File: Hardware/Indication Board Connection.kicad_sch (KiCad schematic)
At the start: 17 parts, among them J18 Conn_01x03, U11 TPS5405DR

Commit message: JLC Production Files
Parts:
- 5V_Buck1: LCSC (none) -> C7371904
- C26, C31, C32, C33: LCSC (none) -> C440198
- C27: LCSC (none) -> C15849
- C28: LCSC (none) -> C57112
- C29: LCSC (none) -> C107088
- C30: LCSC (none) -> C14663
- D27: LCSC (none) -> C41408002
- F1: LCSC (none) -> C269149
- R51: LCSC (none) -> C21190
- R64: LCSC (none) -> C137788
- U11: LCSC (none) -> C488409
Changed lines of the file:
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@@
+			)
+		)
+		(property "LCSC" "C137788"
+			(at 86.868 90.2716 0)
+			(effects
+				(font
+					(size 1.27 1.27)
+				)
+				(hide yes)
 			)
 		)
@@
 			)
 		)
+		(property "LCSC" "C15849"
+			(at 76.6572 63.6016 0)
+			(effects
+				(font
+					(size 1.27 1.27)
+				)
+				(hide yes)
+			)
+		)
 		(pin "1"
 		)
@@
 			)
 		)
+		(property "LCSC" "C107088"
+			(at 88.0872 80.1116 0)
+			(effects
+				(font
+					(size 1.27 1.27)
+				)
+				(hide yes)
+			)
+		)
 		(pin "1"
 		)
@@
 			)
 		)
+		(property "LCSC" "C440198"
+			(at 174.4472 75.0316 0)
+			(effects
+				(font
+					(size 1.27 1.27)
+				)
+				(hide yes)
+			)
+		)
 		(pin "1"
 		)
@@
 		(property "Manufactuerer" "Murata Electronics "
 			(at 182.88 76.2 0)
+			(effects
+				(font
+					(size 1.27 1.27)
+				)
+				(hide yes)
+			)
+		)
+		(property "LCSC" "C440198"
+			(at 185.8772 75.0316 0)
 			(effects
 				(font
@@
 			)
 		)
+		(property "LCSC" "C269149"
+			(at 62.23 132.08 0)
+			(effects
+				(font
+					(size 1.27 1.27)
+				)
+				(hide yes)
+			)
+		)
 		(pin "2"
 		)
@@
 			)
 		)
+		(property "LCSC" "C14663"
+			(at 145.2372 63.6016 0)
+			(effects
+				(font
+					(size 1.27 1.27)
+				)
+				(hide yes)
+			)
+		)
 		(pin "1"
 		)
@@
 			)
 		)
+		(property "LCSC" "C7371904"
+			(at 122.174 146.304 0)
+			(effects
+				(font
+					(size 1.27 1.27)
+				)
+				(hide yes)
+			)
+		)
 		(pin "1"
 		)
@@
 			)
 		)
+		(property "LCSC" "C21190"
+			(at 119.888 133.858 0)
+			(effects
+				(font
+					(size 1.27 1.27)
+				)
+				(hide yes)
+			)
+		)
 		(pin "2"
 		)
@@
 		(property "Manufactuerer" "Murata Electronics "
 			(at 63.5 64.77 0)
+			(effects
+				(font
+					(size 1.27 1.27)
+				)
+				(hide yes)
+			)
+		)
+		(property "LCSC" "C440198"
+			(at 66.4972 63.6016 0)
 			(effects
 				(font
@@
 			)
 		)
+		(property "LCSC" "C440198"
+			(at 163.0172 75.0316 0)
+			(effects
+				(font
+					(size 1.27 1.27)
+				)
+				(hide yes)
+			)
+		)
 		(pin "1"
 		)
@@
 		(property "Manufactuerer" "TAIYO YUDEN "
 			(at 76.2 74.93 0)
+			(effects
+				(font
+					(size 1.27 1.27)
+				)
+				(hide yes)
+			)
+		)
+		(property "LCSC" "C57112"
+			(at 79.1972 73.7616 0)
 			(effects
 				(font
@@
 			)
 		)
+		(property "LCSC" "C41408002"
+			(at 144.78 72.0724 0)
+			(effects
+				(font
+					(size 1.27 1.27)
+				)
+				(hide yes)
+			)
+		)
 		(pin "2"
 		)
@@
 			(effects
 				(font
+					(size 1.27 1.27)
+				)
+				(hide yes)
+			)
+		)
+		(property "LCSC" "C488409"
+			(at 107.95 49.53 0)
+			(effects
+				(font

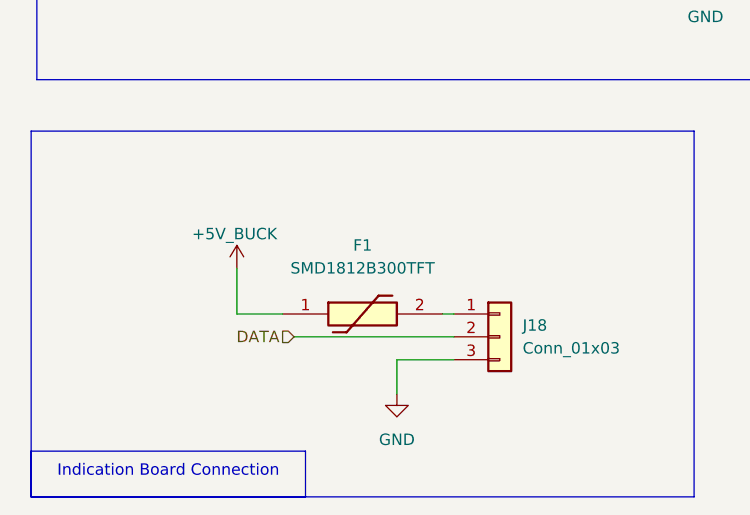
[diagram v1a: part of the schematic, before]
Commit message: condensed custom lirbraries
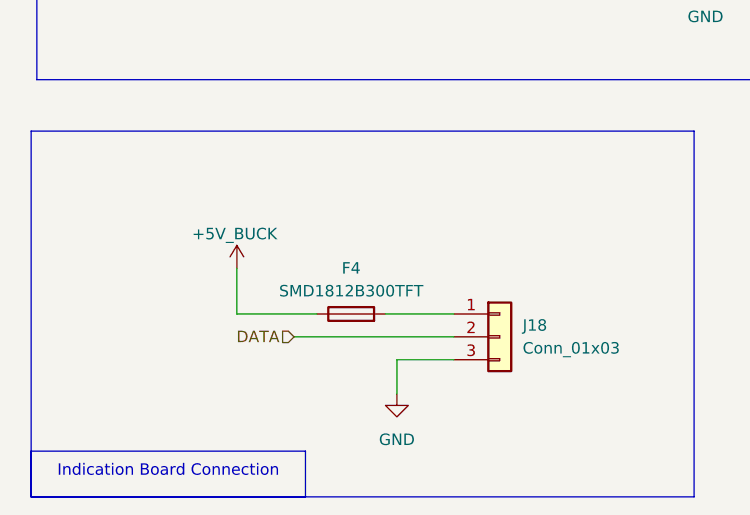
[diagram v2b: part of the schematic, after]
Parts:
- removed F1: SMD1812B300TFT, PTC Fuse:FUSC4632X165N, symbol PTC Fuse:SMD1812B300TFT
- added F4: SMD1812B300TFT, CustomKiCad-Library:FUSC4632X165N, symbol Device:Fuse
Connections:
- net +5V_BUCK: now also F4.1
- net at J18.1 (Pin_1): now also F4.2
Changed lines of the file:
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@@
 	(wire
 		(pts
-			(xy 76.2 78.74) (xy 76.2 80.01)
+			(xy 64.77 139.7) (xy 72.39 139.7)
 		)
 		(stroke
@@
 	(wire
 		(pts
-			(xy 85.09 85.09) (xy 85.09 87.63)
+			(xy 76.2 78.74) (xy 76.2 80.01)
 		)
 		(stroke
@@
 	(wire
 		(pts
-			(xy 128.27 74.93) (xy 130.81 74.93)
+			(xy 85.09 85.09) (xy 85.09 87.63)
 		)
 		(stroke
@@
 	(wire
 		(pts
-			(xy 130.81 82.55) (xy 142.24 82.55)
+			(xy 128.27 74.93) (xy 130.81 74.93)
 		)
 		(stroke
@@
 	(wire
 		(pts
-			(xy 71.12 139.7) (xy 72.39 139.7)
+			(xy 130.81 82.55) (xy 142.24 82.55)
 		)
 		(stroke
@@
 	(wire
 		(pts
-			(xy 48.26 139.7) (xy 53.34 139.7)
+			(xy 48.26 139.7) (xy 57.15 139.7)
 		)
 		(stroke
@@
 	)
 	(symbol
-		(lib_id "PTC Fuse:SMD1812B300TFT")
-		(at 53.34 139.7 0)
-		(unit 1)
-		(exclude_from_sim no)
-		(in_bom yes)
-		(on_board yes)
-		(dnp no)
-		(fields_autoplaced yes)
-		(property "Reference" "F1"
-			(at 62.23 132.08 0)
-			(effects
-				(font
-					(size 1.27 1.27)
-				)
-			)
-		)
-		(property "Value" "SMD1812B300TFT"
-			(at 62.23 134.62 0)
-			(effects
-				(font
-					(size 1.27 1.27)
-				)
-			)
-		)
-		(property "Footprint" "PTC Fuse:FUSC4632X165N"
-			(at 67.31 235.89 0)
-			(effects
-				(font
-					(size 1.27 1.27)
-				)
-				(justify left top)
-				(hide yes)
-			)
-		)
-		(property "Datasheet" "https://www.yageo.com/upload/media/product/productsearch/datasheet/cpc/pptc/SMD1812_1.pdf"
-			(at 67.31 335.89 0)
-			(effects
-				(font
-					(size 1.27 1.27)
-				)
-				(justify left top)
-				(hide yes)
-			)
-		)
-		(property "Description" "Polymeric PTC Resettable Fuse 6V 3 A Ih Surface Mount 1812 (4532 Metric), Concave"
-			(at 53.34 139.7 0)
-			(effects
-				(font
-					(size 1.27 1.27)
-				)
-				(hide yes)
-			)
-		)
-		(property "Height" "1.65"
-			(at 67.31 535.89 0)
-			(effects
-				(font
-					(size 1.27 1.27)
-				)
-				(justify left top)
-				(hide yes)
-			)
-		)
-		(property "Mouser Part Number" "603-SMD1812B300TFT"
-			(at 67.31 635.89 0)
-			(effects
-				(font
-					(size 1.27 1.27)
-				)
-				(justify left top)
-				(hide yes)
-			)
-		)
-		(property "Mouser Price/Stock" "https://www.mouser.co.uk/ProductDetail/YAGEO/SMD1812B300TFT?qs=0lSvoLzn4L%252BUTwukZpvWFw%3D%3D"
-			(at 67.31 735.89 0)
-			(effects
-				(font
-					(size 1.27 1.27)
-				)
-				(justify left top)
-				(hide yes)
-			)
-		)
-		(property "Manufacturer_Name" "YAGEO"
-			(at 67.31 835.89 0)
-			(effects
-				(font
-					(size 1.27 1.27)
-				)
-				(justify left top)
-				(hide yes)
-			)
-		)
-		(property "Manufactuerer" "YAGEO "
-			(at 53.34 139.7 0)
-			(effects
-				(font
-					(size 1.27 1.27)
-				)
-				(hide yes)
-			)
-		)
-		(property "P/N" "SMD1812B300TFT"
-			(at 53.34 139.7 0)
-			(effects
-				(font
-					(size 1.27 1.27)
-				)
-				(hide yes)
-			)
-		)
-		(property "LCSC" "C269149"
-			(at 62.23 132.08 0)
-			(effects
-				(font
-					(size 1.27 1.27)
-				)
-				(hide yes)
-			)
-		)
-		(pin "2"
-		)
-		(pin "1"
-		)
-		(instances
-			(project ""
-				(path "/fb37da34-e420-4994-8cc1-079e8c0fa48e/e5707b84-df8b-4b8b-b215-90bb9859c3b3"
-					(reference "F1")
-					(unit 1)
-				)
-			)
-		)
-	)
-	(symbol
 		(lib_id "Device:C")
 		(at 142.24 64.77 0)
@@
 					(unit 1)
 				)
+			)
+		)
+	)
+	(symbol
+		(lib_id "Device:Fuse")
+		(at 60.96 139.7 90)
+		(unit 1)
+		(exclude_from_sim no)
+		(in_bom yes)
+		(on_board yes)
+		(dnp no)
+		(property "Reference" "F4"
+			(at 60.96 134.62 90)
+			(effects
+				(font
+					(size 1.27 1.27)
+				)
+			)
+		)
+		(property "Value" "SMD1812B300TFT"
+			(at 60.96 137.16 90)
+			(effects
+				(font
+					(size 1.27 1.27)
+				)
+			)
+		)
+		(property "Footprint" "CustomKiCad-Library:FUSC4632X165N"
+			(at 60.96 141.478 90)
+			(effects
+				(font
+					(size 1.27 1.27)
+				)
+				(justify right bottom)
+				(hide yes)
+			)
+		)
+		(property "Datasheet" "https://www.yageo.com/upload/media/product/productsearch/datasheet/cpc/pptc/SMD1812_1.pdf"
+			(at 60.96 139.7 0)
+			(effects
+				(font
+					(size 1.27 1.27)
+				)
+				(justify left top)
+				(hide yes)
+			)
+		)
+		(property "Description" "Polymeric PTC Resettable Fuse 6V 3 A Ih Surface Mount 1812 (4532 Metric), Concave"
+			(at 60.96 139.7 0)
+			(effects
+				(font
+					(size 1.27 1.27)
+				)
+				(hide yes)
+			)
+		)
+		(property "Height" "1.65"
+			(at 60.96 134.62 0)
+			(effects
+				(font
+					(size 1.27 1.27)
+				)
+				(justify left top)
+				(hide yes)
+			)
+		)
+		(property "Mouser Part Number" "603-SMD1812B300TFT"
+			(at 60.96 139.7 90)
+			(effects
+				(font
+					(size 1.27 1.27)
+				)
+				(justify right bottom)
+				(hide yes)
+			)
+		)
+		(property "Mouser Price/Stock" "https://www.mouser.co.uk/ProductDetail/YAGEO/SMD1812B300TFT?qs=0lSvoLzn4L%252BUTwukZpvWFw%3D%3D"
+			(at 60.96 139.7 90)
+			(effects
+				(font
+					(size 1.27 1.27)
+				)
+				(justify right bottom)
+				(hide yes)
+			)
+		)
+		(property "Manufacturer_Name" "YAGEO"
+			(at 60.96 139.7 90)
+			(effects
+				(font
+					(size 1.27 1.27)
+				)
+				(justify right bottom)
+				(hide yes)
+			)
+		)
+		(property "Manufactuerer" "YAGEO "
+			(at 60.96 139.7 90)
+			(effects
+				(font
+					(size 1.27 1.27)
+				)
+				(hide yes)
+			)
+		)
+		(property "P/N" "SMD1812B300TFT"
+			(at 60.96 139.7 90)
+			(effects
+				(font
+					(size 1.27 1.27)
+				)
+				(hide yes)
+			)
+		)
+		(property "LCSC" "C269149"
+			(at 60.96 139.7 90)
+			(effects
+				(font
+					(size 1.27 1.27)
+				)
+				(hide yes)
+			)
+		)
+		(pin "1"
+		)
+		(pin "2"
+		)
+		(instances
+			(project "BPS-Leader"
+				(path "/fb37da34-e420-4994-8cc1-079e8c0fa48e/e5707b84-df8b-4b8b-b215-90bb9859c3b3"
+					(reference "F4")
+					(unit 1)
+				)
